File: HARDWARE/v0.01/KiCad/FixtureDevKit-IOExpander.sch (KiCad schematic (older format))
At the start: 58 parts, among them J83 IOExp_0, J84 IOExp_1, J85 Conn_01x24, J86 Conn_01x24, J87 IOExp_1, J88 IOExp_0, U10 TCA6426A, U9 TCA6426A

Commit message: updating the cover page
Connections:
- net SCL renamed I2C-SDK
- net SDA renamed I2C-SDA
- net VCC-3V3 renamed C4-VCC-4V4
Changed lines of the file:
@@
 $Descr A4 11693 8268
 encoding utf-8
-Sheet 8 10
+Sheet 7 10
 Title ""
 Date ""
@@
 Wire Wire Line
 	8350 5900 8350 5800
+Text HLabel 1300 1250 0    60   BiDi ~ 0
+I2C-SDA
+Text HLabel 1300 1400 0    60   BiDi ~ 0
+I2C-SDK
+Text HLabel 1300 1550 0    60   Input ~ 0
+C4-VCC-4V4
+Text Label 1600 1550 0    60   ~ 0
+VCC-3V3
+Text Label 1600 1250 0    60   ~ 0
+SDA
+Text Label 1600 1400 0    60   ~ 0
+SCL
+Wire Wire Line
+	1300 1250 1600 1250
+Wire Wire Line
+	1300 1400 1600 1400
+Wire Wire Line
+	1300 1550 1600 1550
 $EndSCHEMATC

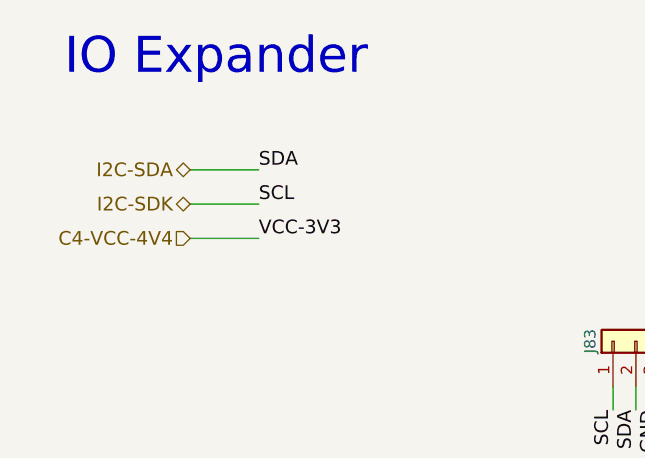
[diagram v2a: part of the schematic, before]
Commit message: adding labelings, hierarchy pins, and page titles
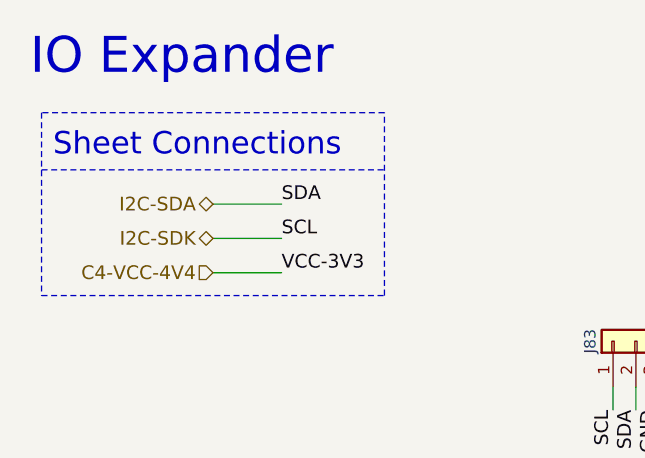
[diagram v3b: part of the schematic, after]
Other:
- note added: "Sheet Connections"
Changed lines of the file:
@@
 encoding utf-8
 Sheet 7 10
-Title ""
-Date ""
-Rev ""
-Comp ""
-Comment1 ""
+Title "IO Expanders"
+Date "2017-10-25"
+Rev "v0.01"
+Comp "Next Thing Co"
+Comment1 "Havin' a Blast!"
 Comment2 ""
 Comment3 ""
@@
 Wire Wire Line
 	7800 3550 7900 3550
-Text Notes 750  850  0    157  ~ 0
+Text Notes 600  850  0    157  ~ 0
 IO Expander
 Wire Wire Line
@@
 Wire Wire Line
 	8350 5900 8350 5800
-Text HLabel 1300 1250 0    60   BiDi ~ 0
+Text HLabel 1400 1400 0    60   BiDi ~ 0
 I2C-SDA
-Text HLabel 1300 1400 0    60   BiDi ~ 0
+Text HLabel 1400 1550 0    60   BiDi ~ 0
 I2C-SDK
-Text HLabel 1300 1550 0    60   Input ~ 0
+Text HLabel 1400 1700 0    60   Input ~ 0
 C4-VCC-4V4
-Text Label 1600 1550 0    60   ~ 0
+Text Label 1700 1700 0    60   ~ 0
 VCC-3V3
-Text Label 1600 1250 0    60   ~ 0
+Text Label 1700 1400 0    60   ~ 0
 SDA
-Text Label 1600 1400 0    60   ~ 0
+Text Label 1700 1550 0    60   ~ 0
 SCL
 Wire Wire Line
-	1300 1250 1600 1250
-Wire Wire Line
-	1300 1400 1600 1400
-Wire Wire Line
-	1300 1550 1600 1550
+	1400 1400 1700 1400
+Wire Wire Line
+	1400 1550 1700 1550
+Wire Wire Line
+	1400 1700 1700 1700
+Text Notes 700  1200 0    98   ~ 0
+Sheet Connections
+Wire Notes Line
+	650  1000 650  1800
+Wire Notes Line
+	650  1800 2150 1800
+Wire Notes Line
+	2150 1800 2150 1000
+Wire Notes Line
+	2150 1000 650  1000
+Wire Notes Line
+	650  1250 2150 1250
 $EndSCHEMATC

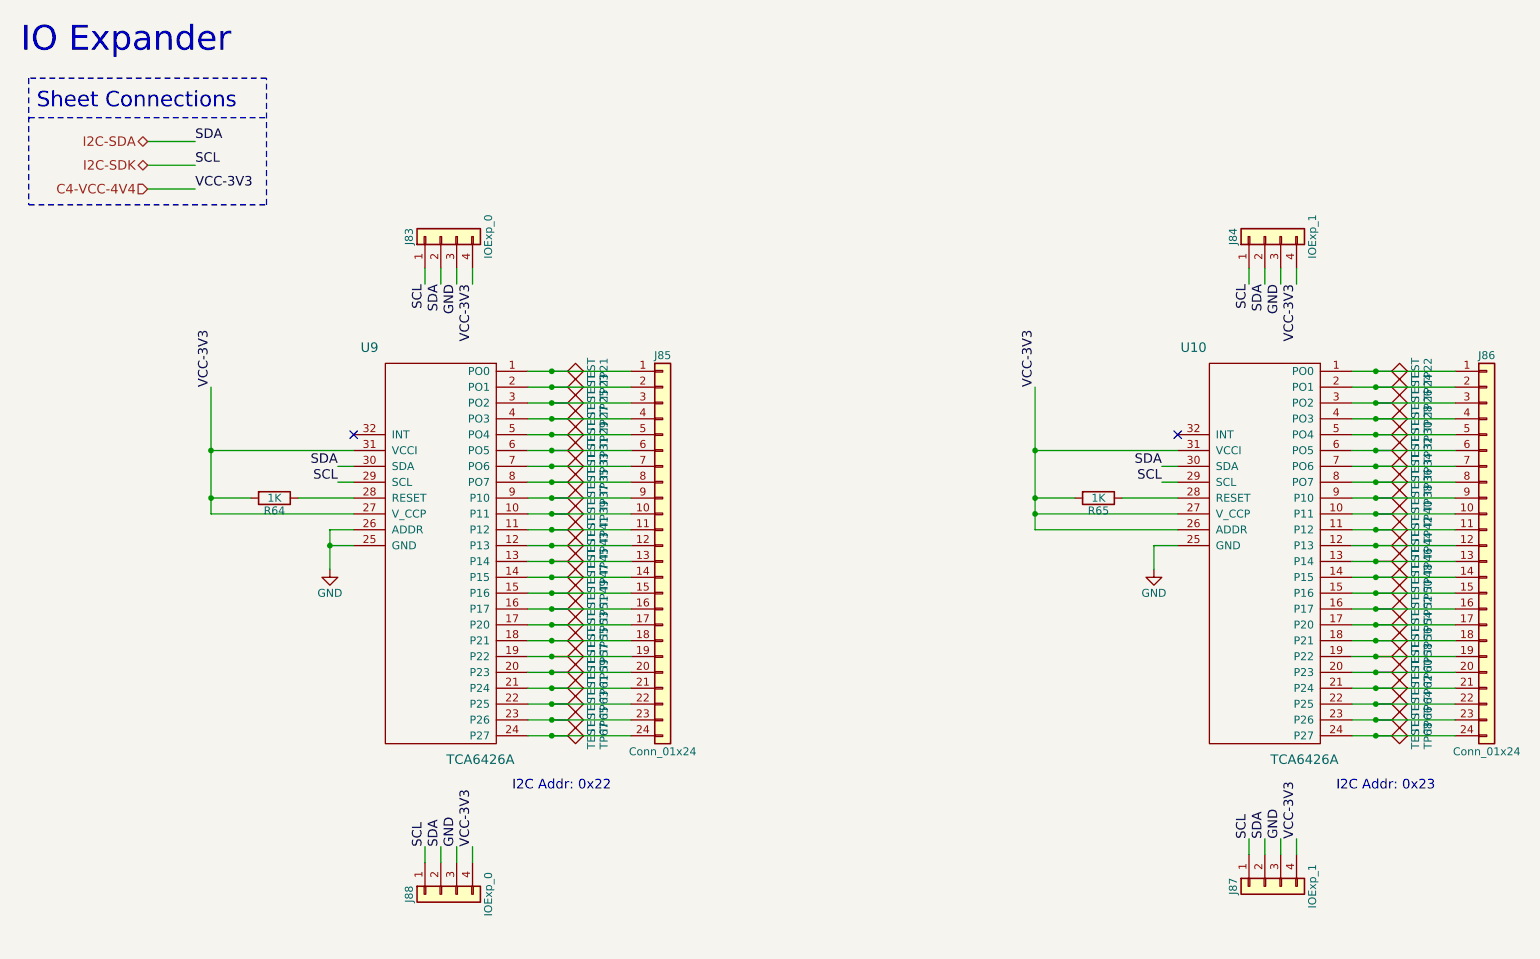
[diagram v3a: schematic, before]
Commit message: adjusting page sizes and cleaning up schematics
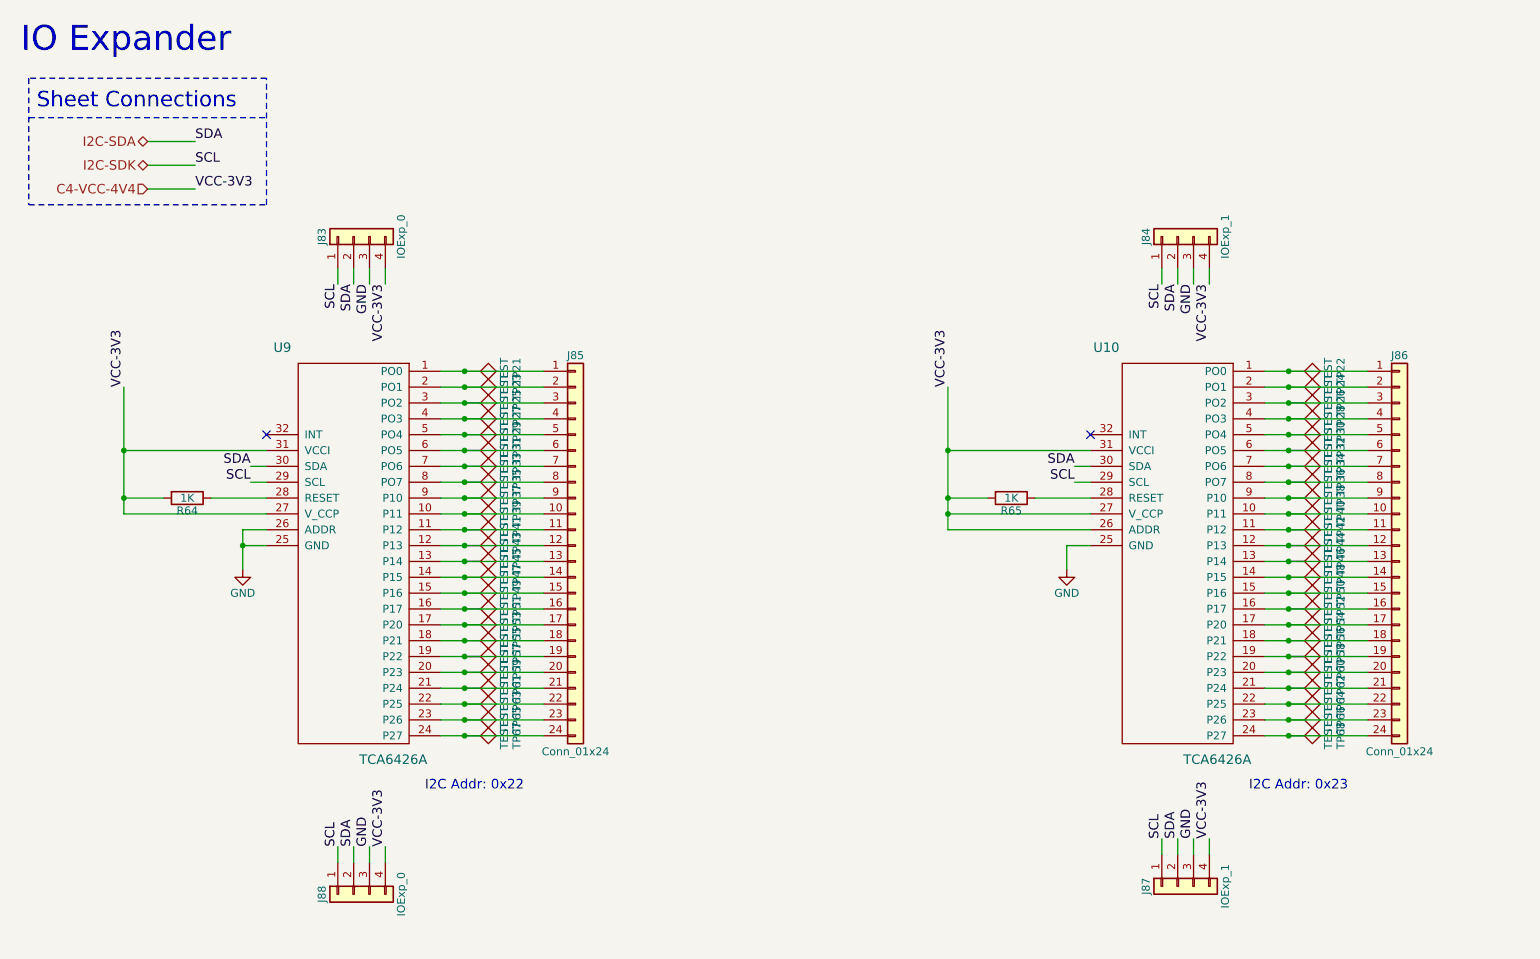
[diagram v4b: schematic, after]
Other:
- moved on the sheet: J83, J84, J85, J86, J87, J88, R64, R65, TP21, TP22, TP23, TP24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

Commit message: cleaning up schematic, run rules check, generate net list
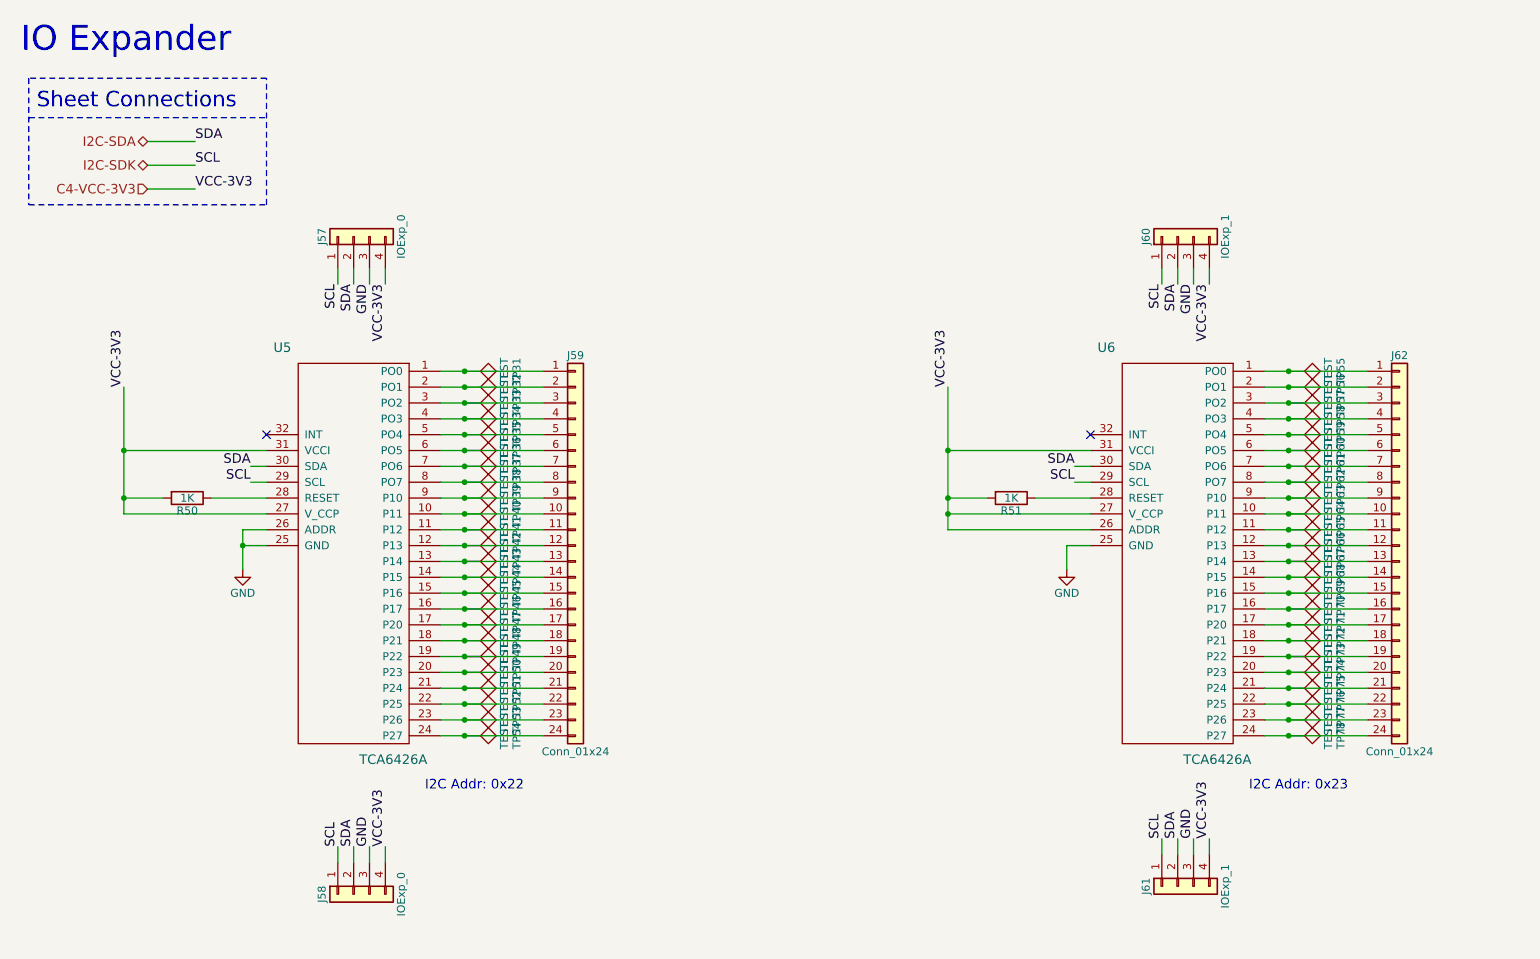
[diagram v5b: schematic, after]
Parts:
- renumbered J83 to J57, J88 to J58, J85 to J59, J84 to J60, J87 to J61, J86 to J62, R64 to R50, R65 to R51, TP21 to TP31, TP23 to TP32, TP25 to TP33, TP27 to TP34, TP29 to TP35, TP31 to TP36, TP33 to TP37, TP35 to TP38, TP37 to TP39, TP39 to TP40, TP43 to TP42, TP45 to TP43, TP47 to TP44, TP49 to TP45, TP51 to TP46, TP53 to TP47, TP55 to TP48, TP57 to TP49, TP59 to TP50, TP61 to TP51, TP63 to TP52, TP65 to TP53, TP67 to TP54, TP22 to TP55, TP24 to TP56, TP26 to TP57, TP28 to TP58, TP30 to TP59, TP32 to TP60, TP34 to TP61, TP36 to TP62, TP38 to TP63, TP40 to TP64, TP42 to TP65, TP44 to TP66, TP46 to TP67, TP48 to TP68, TP50 to TP69, TP52 to TP70, TP54 to TP71, TP56 to TP72, TP58 to TP73, TP60 to TP74, TP62 to TP75, TP64 to TP76, TP66 to TP77, TP68 to TP78, U9 to U5, U10 to U6
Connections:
- net C4-VCC-4V4 renamed C4-VCC-3V3

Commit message: adding footprints
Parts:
- J57, J58, J60, J61: footprint (none) -> Pin_Headers:Pin_Header_Straight_1x04_Pitch2.54mm
- J59, J62: footprint (none) -> Pin_Headers:Pin_Header_Straight_1x24_Pitch2.54mm
- R50, R51: footprint (none) -> Resistors_SMD:R_0805_HandSoldering
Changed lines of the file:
@@
 F 0 "J59" H 4100 5150 50  0000 C CNN
 F 1 "Conn_01x24" H 4100 2650 50  0000 C CNN
-F 2 "" H 4100 3950 50  0001 C CNN
+F 2 "Pin_Headers:Pin_Header_Straight_1x24_Pitch2.54mm" H 4100 3950 50  0001 C CNN
 F 3 "" H 4100 3950 50  0001 C CNN
 	1    4100 3950
@@
 F 0 "R50" V 1730 3650 50  0000 C CNN
 F 1 "1K" V 1650 3650 50  0000 C CNN
-F 2 "" V 1580 3650 50  0001 C CNN
+F 2 "Resistors_SMD:R_0805_HandSoldering" V 1580 3650 50  0001 C CNN
 F 3 "" H 1650 3650 50  0001 C CNN
 	1    1650 3650
@@
 F 0 "J57" H 2700 2200 50  0000 C CNN
 F 1 "IOExp_0" H 2700 1700 50  0000 C CNN
-F 2 "" H 2700 2000 50  0001 C CNN
+F 2 "Pin_Headers:Pin_Header_Straight_1x04_Pitch2.54mm" H 2700 2000 50  0001 C CNN
 F 3 "" H 2700 2000 50  0001 C CNN
 	1    2700 2000
@@
 F 0 "J62" H 9300 5150 50  0000 C CNN
 F 1 "Conn_01x24" H 9300 2650 50  0000 C CNN
-F 2 "" H 9300 3950 50  0001 C CNN
+F 2 "Pin_Headers:Pin_Header_Straight_1x24_Pitch2.54mm" H 9300 3950 50  0001 C CNN
 F 3 "" H 9300 3950 50  0001 C CNN
 	1    9300 3950
@@
 F 0 "R51" V 6930 3650 50  0000 C CNN
 F 1 "1K" V 6850 3650 50  0000 C CNN
-F 2 "" V 6780 3650 50  0001 C CNN
+F 2 "Resistors_SMD:R_0805_HandSoldering" V 6780 3650 50  0001 C CNN
 F 3 "" H 6850 3650 50  0001 C CNN
 	1    6850 3650
@@
 F 0 "J58" H 2700 6350 50  0000 C CNN
 F 1 "IOExp_0" H 2700 5850 50  0000 C CNN
-F 2 "" H 2700 6150 50  0001 C CNN
+F 2 "Pin_Headers:Pin_Header_Straight_1x04_Pitch2.54mm" H 2700 6150 50  0001 C CNN
 F 3 "" H 2700 6150 50  0001 C CNN
 	1    2700 6150
@@
 F 0 "J60" H 7900 2200 50  0000 C CNN
 F 1 "IOExp_1" H 7900 1700 50  0000 C CNN
-F 2 "" H 7900 2000 50  0001 C CNN
+F 2 "Pin_Headers:Pin_Header_Straight_1x04_Pitch2.54mm" H 7900 2000 50  0001 C CNN
 F 3 "" H 7900 2000 50  0001 C CNN
 	1    7900 2000
@@
 F 0 "J61" H 7900 6300 50  0000 C CNN
 F 1 "IOExp_1" H 7900 5800 50  0000 C CNN
-F 2 "" H 7900 6100 50  0001 C CNN
+F 2 "Pin_Headers:Pin_Header_Straight_1x04_Pitch2.54mm" H 7900 6100 50  0001 C CNN
 F 3 "" H 7900 6100 50  0001 C CNN
 	1    7900 6100
